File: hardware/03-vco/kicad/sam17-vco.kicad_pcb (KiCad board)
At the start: 4 copper layers, 114 x 124 mm, 140 parts, among them J1 Molex_KK-254_AE-6410-04A_1x04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, J2 IDC-Header_2x06_P2.54mm_Verti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, U1 QFN-32-1EP_4x4mm_P0.4mm_EP2.6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, U10 SOIC-14_3.9x8.7mm_P1.27mm, U11 SOT-89-3, U12 SOT-223-3_TabPin2, U13 VSSOP-8_3x3mm_P0.65mm, U14 SOT-23-5, U2 QFN-32-1EP_4x4mm_P0.4mm_EP2.6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, U3 QFN-32-1EP_4x4mm_P0.4mm_EP2.6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, U4 QFN-32-1EP_4x4mm_P0.4mm_EP2.6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, U5 TSSOP-16_4.4x5mm_P0.65mm, U6 TSSOP-16_4.4x5mm_P0.65mm, U7 TSSOP-16_4.4x5mm_P0.65mm, U8 SOIC-8_3.9x4.9mm_P1.27mm, U9 SOIC-14_3.9x8.7mm_P1.27mm

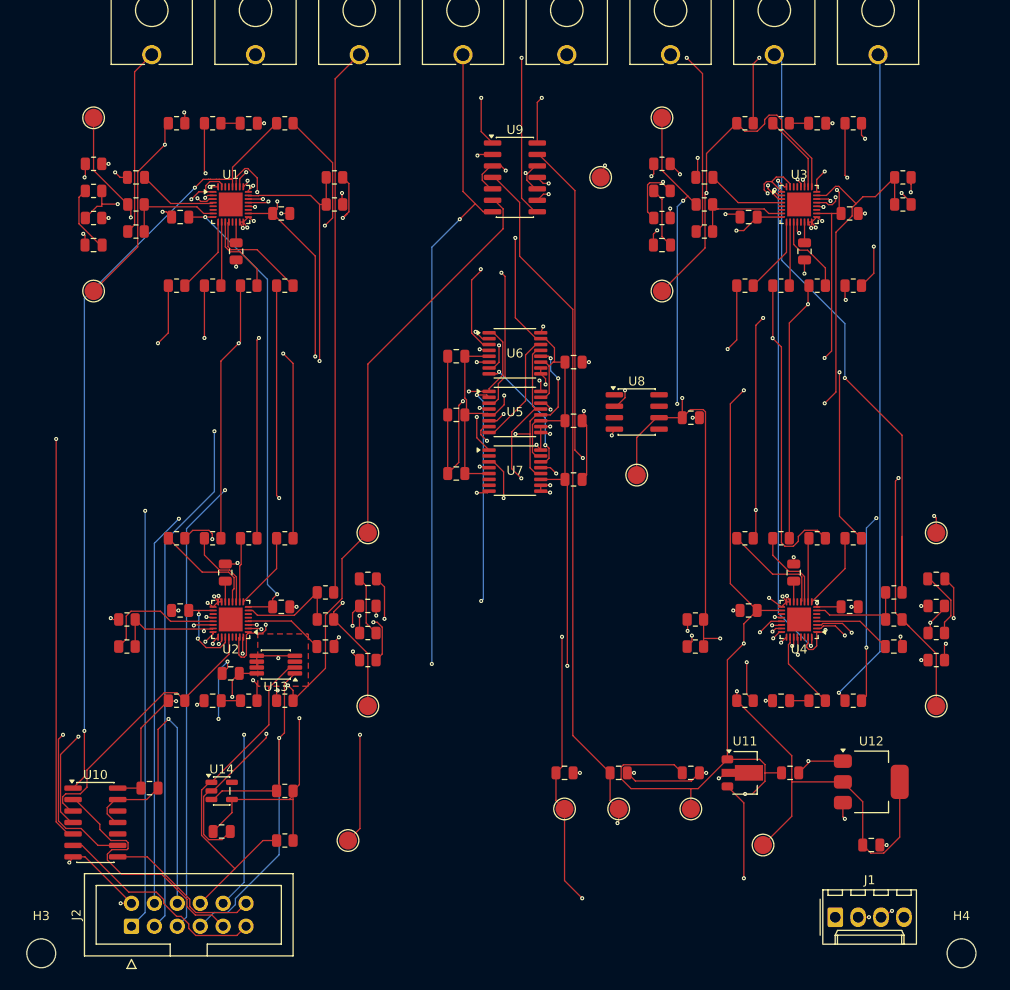
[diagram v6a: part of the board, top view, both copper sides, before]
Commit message: La placa del modulo 3 vuelve a cerrar, con las ocho piezas dentro y una puerta nueva para que no se pueda volver a hacer sin ellas
El septimo fallo de la familia que arregla esta rama, y el peor: los otros seis
mentian sobre si habian comprobado algo. Este dejaba pasar una placa
fisicamente distinta del esquematico con todas las luces en verde.

colocar() itera sobre COLOCACION, un diccionario de posiciones escrito a mano.
C_IV1-4 y R_OUT1-4 no estaban ahi, asi que quedaron fuera SIN UNA PALABRA. La
placa salio con 136 huellas contra 144 componentes, Freerouting cerro con CERO
tramos al aire y el DRC dio 0 infracciones. Lo cazo netdiff, o sea media hora
tarde, y solo porque el cruce esquematico <-> placa existe.

La causa es un proxy de manual (Principio IV): check_huellas() PARECE que
verifica huellas y lo que verifica es que los ficheros .kicad_mod existan en
disco. Nunca miro si cada componente tenia donde ir.

check_cobertura() exige que COLOCACION cubra el netlist en los dos sentidos y
aborta antes de crear un solo objeto. Su mutacion mordio en el estado que ya
sabiamos roto, nombrando los ocho.

Colocacion: C_IV en la MISMA columna que su R_IV y a 4 mm, el paso que usa el
resto de la fila. Los dos estan en paralelo y forman el lazo de
realimentacion, asi que el area que encierran es circuito, no estetica. R_OUT
al lado, que vive fuera del lazo y no tiene esa exigencia.

Dos cosas mas que salieron de medir, no de tantear:

COSTURAS_RESERVADAS pasa de 7 a 12. Con las ocho piezas nuevas el centro se
congestiono y dos pines de masa se quedaron sin camino hasta el plano -- no sin
DISTANCIA: habia vias de GNDA a 3.27 y 5.39 mm de U9.12, y a 1.60 mm de U7.16.
Lo que faltaba era por donde pasar, porque el router llega antes. Entran las
CUATRO entradas + de U9 (pines 3, 5, 10, 12), no solo la que fallo: en un
amplificador de transimpedancia esa entrada ES la referencia que define el
punto virtual, su impedancia hasta el plano forma parte del circuito, y cual de
las cua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
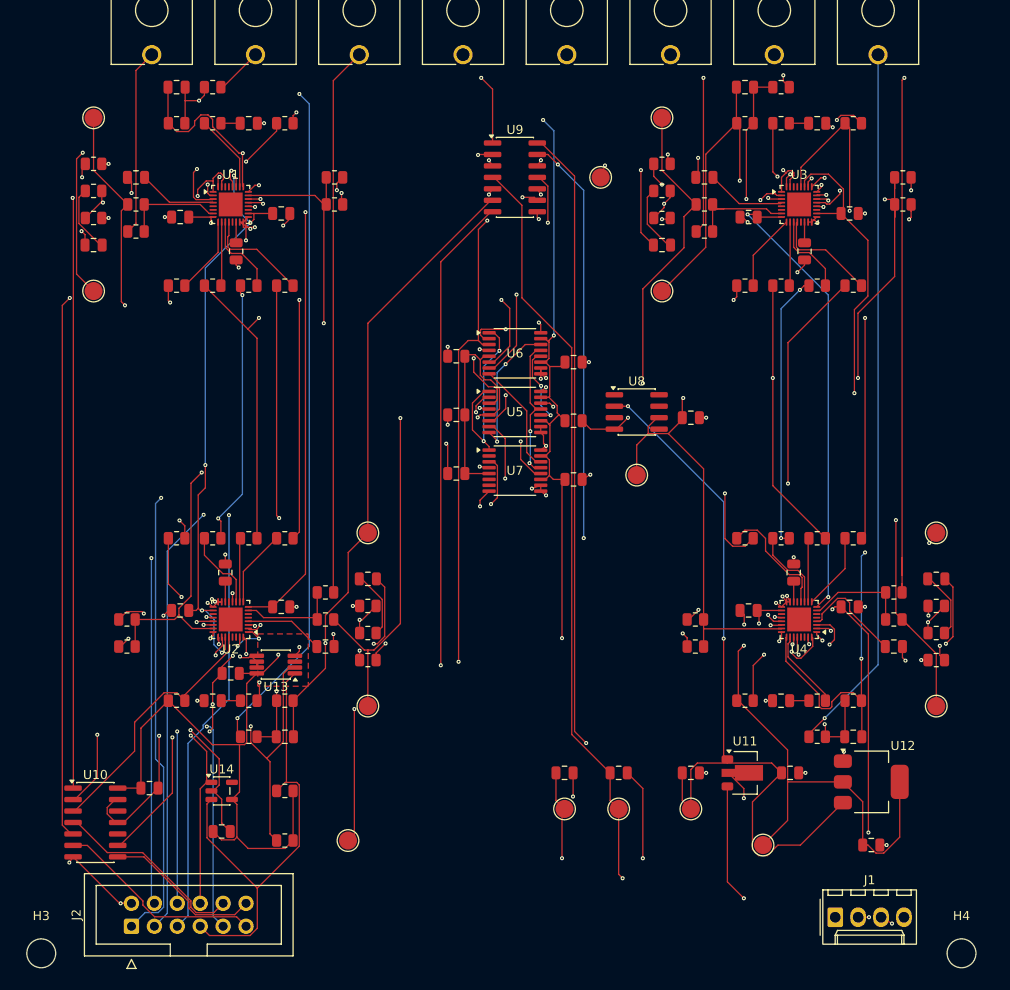
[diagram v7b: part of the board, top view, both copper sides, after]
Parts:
- added C_IV1: C_0805_2012Metric, C_0805_2012Metric, F.Cu at (21.0, 22.0)
- added C_IV2: C_0805_2012Metric, C_0805_2012Metric, F.Cu at (33.0, 94.0)
- added C_IV3: C_0805_2012Metric, C_0805_2012Metric, F.Cu at (84.0, 22.0)
- added C_IV4: C_0805_2012Metric, C_0805_2012Metric, F.Cu at (96.0, 94.0)
- added R_OUT1: R_0805_2012Metric, R_0805_2012Metric, F.Cu at (25.0, 22.0)
- added R_OUT2: R_0805_2012Metric, R_0805_2012Metric, F.Cu at (29.0, 94.0)
- added R_OUT3: R_0805_2012Metric, R_0805_2012Metric, F.Cu at (88.0, 22.0)
- added R_OUT4: R_0805_2012Metric, R_0805_2012Metric, F.Cu at (92.0, 94.0)
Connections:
- R_IV1 pad 2: VOICE_OUT_1 -> IVO_1
- R_IV2 pad 2: VOICE_OUT_2 -> IVO_2
- R_IV3 pad 2: VOICE_OUT_3 -> IVO_3
- R_IV4 pad 2: VOICE_OUT_4 -> IVO_4
- U9 pad 1: VOICE_OUT_1 -> IVO_1
- U9 pad 14: VOICE_OUT_4 -> IVO_4
- U9 pad 7: VOICE_OUT_2 -> IVO_2
- U9 pad 8: VOICE_OUT_3 -> IVO_3
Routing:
- net IVO_4: track 0.00 -> 103.9 mm, vias 0 -> 2
- net IVO_2: track 0.00 -> 79.4 mm, vias 0 -> 2
- net IVO_1: track 0.00 -> 47.4 mm, vias 0 -> 2
- net IVO_3: track 0.00 -> 39.7 mm, vias 0 -> 2
- net VOICE_OUT_4: track 118.3 -> 78.8 mm, vias 2 -> 1
- net VOICE_OUT_1: track 44.3 -> 5.33 mm, vias 2 -> 0
- net VOICE_OUT_3: track 53.2 -> 15.0 mm, vias 2 -> 1
- net TUNE_OUT_2: track 49.1 -> 21.6 mm, vias 2 -> 0
- net GNDA: track 136.9 -> 111.5 mm, vias 79 -> 81
- net MIXO_1: track 62.7 -> 81.7 mm
- net SQ_3: track 151.8 -> 169.8 mm, vias 3 -> 2
- net PWM_CV: track 206.9 -> 190.6 mm, vias 5 -> 6
- net TUNE_OUT_1: track 28.6 -> 44.0 mm, vias 0 -> 2
- net MIXO_3: track 56.5 -> 70.7 mm, vias 2 -> 3
- net SQ_4: track 109.2 -> 95.7 mm
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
